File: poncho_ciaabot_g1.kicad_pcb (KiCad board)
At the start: 2 copper layers, 26 parts, among them IC1 LM2577HV-ADJ, J1 CONN_01X02, J2 MOT_A, J3 MOT_B, J4 CONN_02X04, J5 CONN_01X03, J6 CONN_01X03, J7 CONN_01X03, J8 CONN_01X02, U1 POLOLU_A4988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

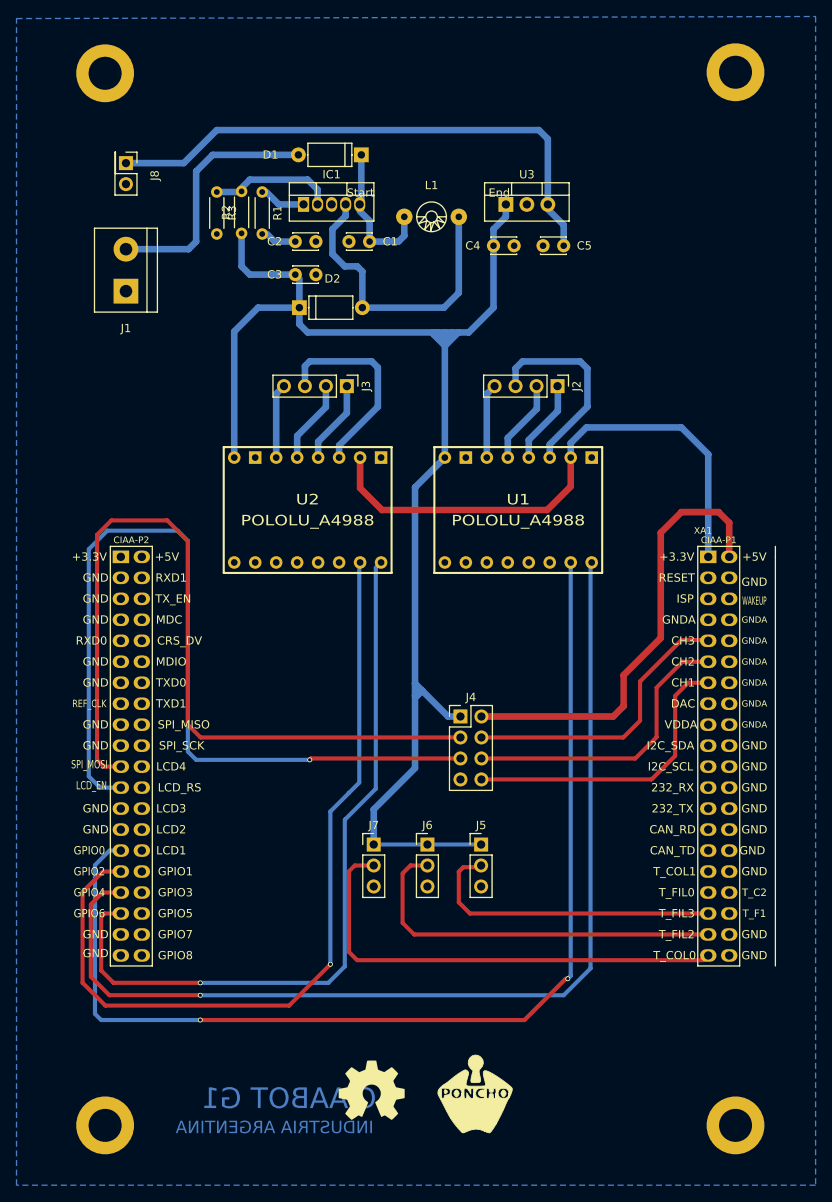
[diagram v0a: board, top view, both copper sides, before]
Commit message: Se agrega borde PCB
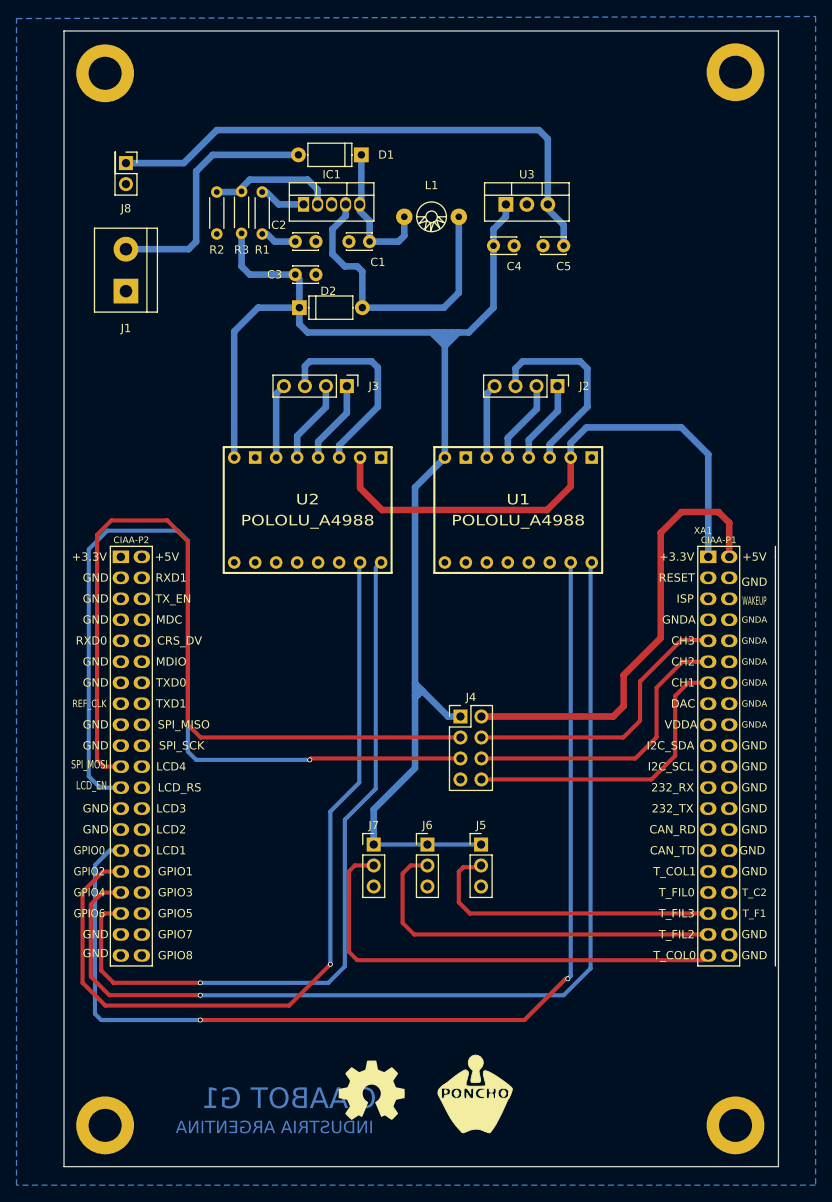
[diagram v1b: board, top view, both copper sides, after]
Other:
- board outline added: 86.5 x 137.5 mm
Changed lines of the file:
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@@
     (links 75)
     (no_connects 0)
-    (area 36.75 12.75 133.500001 154.250001)
+    (area 106.75 19.75 203.500001 161.250001)
     (thickness 1.6)
-    (drawings 2)
+    (drawings 6)
     (tracks 243)
     (zones 0)
@@
     (descr "C, Disc series, Radial, pin pitch=2.50mm, , diameter*width=3*2mm^2, Capacitor")
     (tags "C Disc series Radial pin pitch 2.50mm  diameter 3mm width 2mm Capacitor")
-    (fp_text reference C1 (at -2.5 0 180) (layer F.SilkS)
+    (fp_text reference C1 (at -1 -2.5 180) (layer F.SilkS)
       (effects (font (size 1 1) (thickness 0.15)))
     )
@@
     (descr "C, Disc series, Radial, pin pitch=2.50mm, , diameter*width=3*2mm^2, Capacitor")
     (tags "C Disc series Radial pin pitch 2.50mm  diameter 3mm width 2mm Capacitor")
-    (fp_text reference C2 (at -2.5 0) (layer F.SilkS)
+    (fp_text reference C2 (at -2 -2) (layer F.SilkS)
       (effects (font (size 1 1) (thickness 0.15)))
     )
@@
     (descr "C, Disc series, Radial, pin pitch=2.50mm, , diameter*width=3*2mm^2, Capacitor")
     (tags "C Disc series Radial pin pitch 2.50mm  diameter 3mm width 2mm Capacitor")
-    (fp_text reference C4 (at -2.5 0) (layer F.SilkS)
+    (fp_text reference C4 (at 2.5 2.5) (layer F.SilkS)
       (effects (font (size 1 1) (thickness 0.15)))
     )
@@
     (descr "C, Disc series, Radial, pin pitch=2.50mm, , diameter*width=3*2mm^2, Capacitor")
     (tags "C Disc series Radial pin pitch 2.50mm  diameter 3mm width 2mm Capacitor")
-    (fp_text reference C5 (at -2.5 0 180) (layer F.SilkS)
+    (fp_text reference C5 (at 0 -2.5 180) (layer F.SilkS)
       (effects (font (size 1 1) (thickness 0.15)))
     )
@@
     (fp_circle (center 0 0) (end 0.70104 0) (layer F.SilkS) (width 0.15))
     (fp_circle (center 0 0) (end 1.80086 0) (layer F.SilkS) (width 0.15))
-    (fp_text user End (at 8.19912 -2.90068) (layer F.SilkS)
-      (effects (font (size 1 1) (thickness 0.15)))
-    )
-    (fp_text user Start (at -8.60044 -2.90068) (layer F.SilkS)
-      (effects (font (size 1 1) (thickness 0.15)))
-    )
     (pad 1 thru_hole circle (at -3.29946 0) (size 1.99898 1.99898) (drill 0.8001) (layers *.Cu *.Mask)
       (net 1 +BATT))
@@
     (descr "Resistor, Axial_DIN0204 series, Axial, Horizontal, pin pitch=5.08mm, 0.16666666666666666W = 1/6W, length*diameter=3.6*1.6mm^2, http://cdn-reichelt.de/documents/datenblatt/B400/1_4W%23YAG.pdf")
     (tags "Resistor Axial_DIN0204 series Axial Horizontal pin pitch 5.08mm 0.16666666666666666W = 1/6W length 3.6mm diameter 1.6mm")
-    (fp_text reference R1 (at 2.54 -1.86 270) (layer F.SilkS)
+    (fp_text reference R1 (at 7 0 360) (layer F.SilkS)
       (effects (font (size 1 1) (thickness 0.15)))
     )
@@
     (descr "Resistor, Axial_DIN0204 series, Axial, Horizontal, pin pitch=5.08mm, 0.16666666666666666W = 1/6W, length*diameter=3.6*1.6mm^2, http://cdn-reichelt.de/documents/datenblatt/B400/1_4W%23YAG.pdf")
     (tags "Resistor Axial_DIN0204 series Axial Horizontal pin pitch 5.08mm 0.16666666666666666W = 1/6W length 3.6mm diameter 1.6mm")
-    (fp_text reference R2 (at 2.54 -1.86 90) (layer F.SilkS)
+    (fp_text reference R2 (at -2 -3 180) (layer F.SilkS)
       (effects (font (size 1 1) (thickness 0.15)))
     )
@@
     (descr "Resistor, Axial_DIN0204 series, Axial, Horizontal, pin pitch=5.08mm, 0.16666666666666666W = 1/6W, length*diameter=3.6*1.6mm^2, http://cdn-reichelt.de/documents/datenblatt/B400/1_4W%23YAG.pdf")
     (tags "Resistor Axial_DIN0204 series Axial Horizontal pin pitch 5.08mm 0.16666666666666666W = 1/6W length 3.6mm diameter 1.6mm")
-    (fp_text reference R3 (at 2.54 -1.86 270) (layer F.SilkS)
+    (fp_text reference R3 (at 7 -3 360) (layer F.SilkS)
       (effects (font (size 1 1) (thickness 0.15)))
     )
@@
     (descr "Through hole straight pin header, 1x04, 2.54mm pitch, single row")
     (tags "Through hole pin header THT 1x04 2.54mm single row")
-    (fp_text reference J2 (at 0 -2.33 270) (layer F.SilkS)
+    (fp_text reference J2 (at 0 -3.25 360) (layer F.SilkS)
       (effects (font (size 1 1) (thickness 0.15)))
     )
@@
     (descr "Through hole straight pin header, 1x04, 2.54mm pitch, single row")
     (tags "Through hole pin header THT 1x04 2.54mm single row")
-    (fp_text reference J3 (at 0 -2.33 270) (layer F.SilkS)
+    (fp_text reference J3 (at 0 -3.25 360) (layer F.SilkS)
       (effects (font (size 1 1) (thickness 0.15)))
     )
@@
     (descr "Through hole straight pin header, 2x01, 2.54mm pitch, double rows")
     (tags "Through hole pin header THT 2x01 2.54mm double row")
-    (fp_text reference J8 (at 1.5 -3.5 270) (layer F.SilkS)
+    (fp_text reference J8 (at 5.5 0 360) (layer F.SilkS)
       (effects (font (size 1 1) (thickness 0.15)))
     )
@@
     (descr "D, A-405 series, Axial, Horizontal, pin pitch=7.62mm, , length*diameter=5.2*2.7mm^2, , http://www.diodes.com/_files/packages/A-405.pdf")
     (tags "D A-405 series Axial Horizontal pin pitch 7.62mm  length 5.2mm diameter 2.7mm")
-    (fp_text reference D1 (at 11 0 180) (layer F.SilkS)
+    (fp_text reference D1 (at -3 0 180) (layer F.SilkS)
       (effects (font (size 1 1) (thickness 0.15)))
     )
@@
     (descr "D, A-405 series, Axial, Horizontal, pin pitch=7.62mm, , length*diameter=5.2*2.7mm^2, , http://www.diodes.com/_files/packages/A-405.pdf")
     (tags "D A-405 series Axial Horizontal pin pitch 7.62mm  length 5.2mm diameter 2.7mm")
-    (fp_text reference D2 (at 4 -3.5) (layer F.SilkS)
+    (fp_text reference D2 (at 3.5 -2) (layer F.SilkS)
       (effects (font (size 1 1) (thickness 0.15)))
     )
@@
       (xy 3.778435 -0.1467) (xy 3.778435 -0.1467)) (layer F.SilkS) (width 0.1))
   )
+  (gr_line (start 112.5 159) (end 112.5 21.5) (angle 90) (layer Edge.Cuts) (width 0.15))
+  (gr_line (start 199 159) (end 112.5 159) (angle 90) (layer Edge.Cuts) (width 0.15))
+  (gr_line (start 199 21.5) (end 199 159) (angle 90) (layer Edge.Cuts) (width 0.15))
+  (gr_line (start 112.5 21.5) (end 199 21.5) (angle 90) (layer Edge.Cuts) (width 0.15))
   (gr_text "CIAABOT G1" (at 139.75 150.75) (layer B.Cu)
     (effects (font (size 2.5 2.5) (thickness 0.5)) (justify mirror))
